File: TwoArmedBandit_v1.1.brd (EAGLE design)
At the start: 165.1 x 101.6 mm, 37 parts, among them J1 Nose_L, J10 LED_L, J11 Nose_R, J12 Lick_R, J13 Aux, J14 POWER_JACK, J15 Valve_R, J16 DAQ_L, J17 LED_R, J18 V_valve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

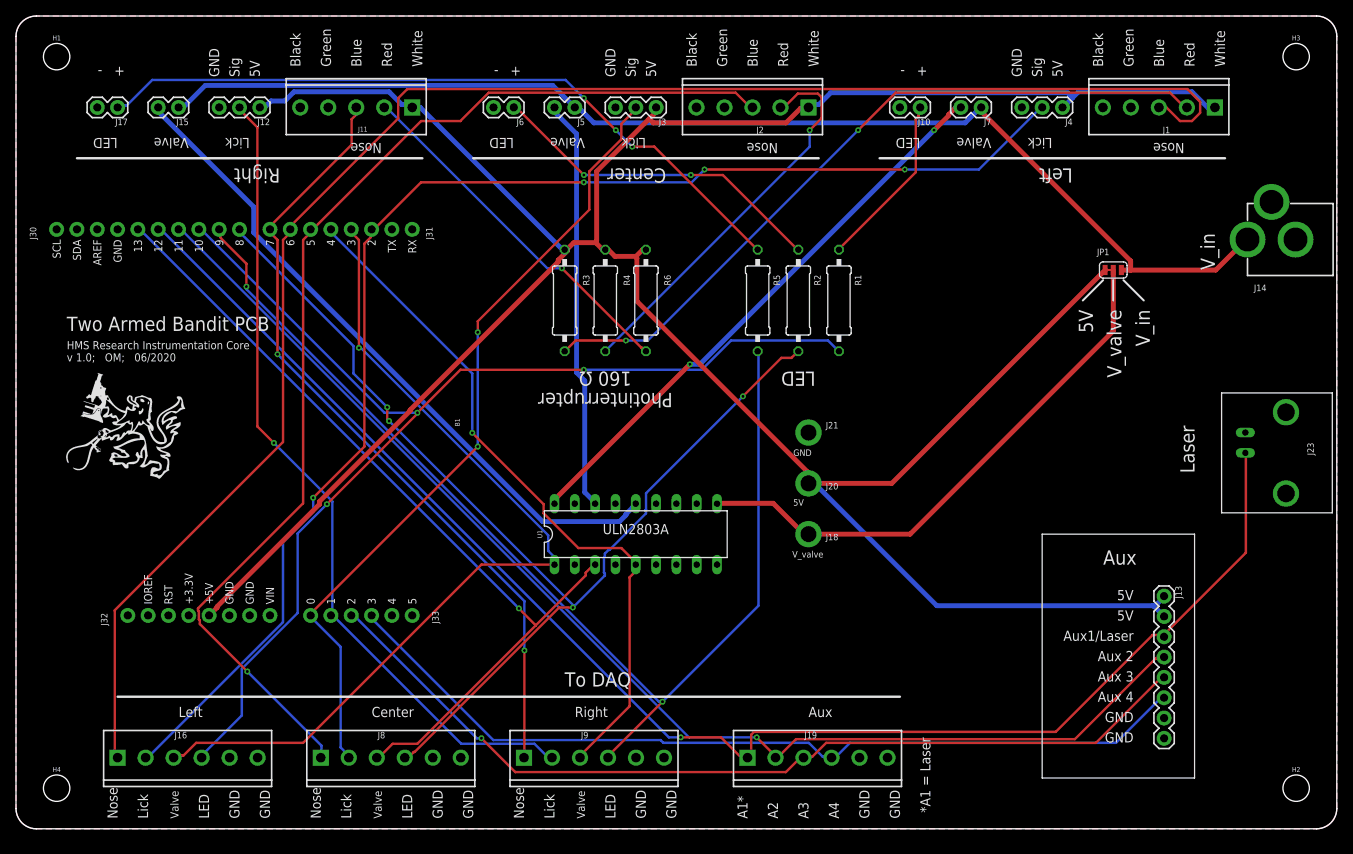
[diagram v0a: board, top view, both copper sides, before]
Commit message: Fix wiring of V_valve; Update version to v1.1
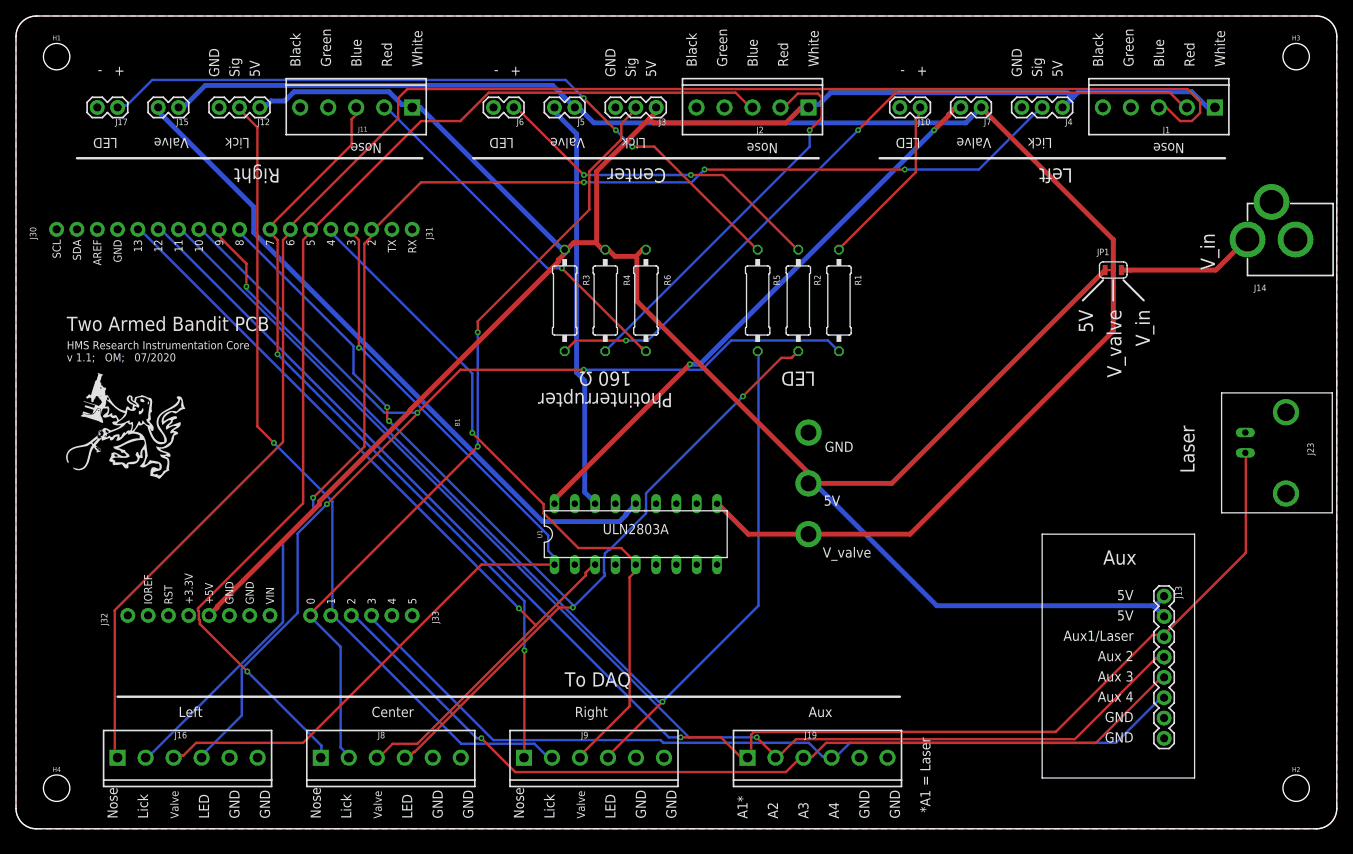
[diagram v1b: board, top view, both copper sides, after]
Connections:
- removed net VCC: J18.1, JP1.2, U1.10
- new net V_VALVE: J15.1, J18.1, J5.1, J7.1, JP1.2, U1.10
- net VIN: no longer J15.1, J5.1, J7.1
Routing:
- net V_VALVE: track 0.00 -> 200.6 mm
- net VIN: track 149.7 -> 17.4 mm
- net VCC: track 69.4 -> 0.00 mm
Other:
- board text added: "HMS Research Instrumentation Core v 1.1; OM; 07/2020"
- board text removed: "HMS Research Instrumentation Core v 1.0; OM; 06/2020"
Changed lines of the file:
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@@
 <text x="6.35" y="62.23" size="1.778" layer="21" font="vector" ratio="15">Two Armed Bandit PCB</text>
 <text x="6.35" y="58.42" size="1.016" layer="21" font="vector" ratio="13">HMS Research Instrumentation Core
-v 1.0;   OM;   06/2020</text>
+v 1.1;   OM;   07/2020</text>
 <text x="77.47" y="36.83" size="1.27" layer="21" font="vector" rot="SR0" align="bottom-center">ULN2803A</text>
 <text x="2.54" y="73.66" size="0.8128" layer="21" font="vector" ratio="15" rot="R90">J30</text>
@@
 </element>
 <element name="FRAME1" library="SparkFun-Aesthetics" library_urn="urn:adsk.eagle:library:507" package="DUMMY" package3d_urn="urn:adsk.eagle:package:37104/1" value="FRAME-LETTERNO_PACKAGE" x="-5.08" y="-2.54" smashed="yes" rot="R180">
-<attribute name="DESIGNER" value="Nobody" x="-5.08" y="-2.54" size="1.778" layer="27" rot="R180" display="off"/>
-<attribute name="VERSION" value="v01" x="-5.08" y="-2.54" size="1.778" layer="27" rot="R180" display="off"/>
+<attribute name="DESIGNER" value="Ofer Mazor" x="-5.08" y="-2.54" size="1.778" layer="27" rot="R180" display="off"/>
+<attribute name="VERSION" value="v01.1" x="-5.08" y="-2.54" size="1.778" layer="27" rot="R180" display="off"/>
 </element>
 <element name="J1" library="SparkFun-Connectors" library_urn="urn:adsk.eagle:library:513" package="SCREWTERMINAL-3.5MM-5" package3d_urn="urn:adsk.eagle:package:38112/1" value="Nose_L" x="149.86" y="90.17" smashed="yes" rot="R180">
@@
 </element>
 <element name="J18" library="SparkFun-Connectors" library_urn="urn:adsk.eagle:library:513" package="1X01_2MM" package3d_urn="urn:adsk.eagle:package:38029/1" value="V_valve" x="99.06" y="36.83" smashed="yes">
-<attribute name="NAME" x="101.219" y="36.068" size="0.8128" layer="25" font="vector" ratio="15"/>
-<attribute name="VALUE" x="97.028" y="33.909" size="0.8128" layer="21" font="vector" ratio="15"/>
+<attribute name="VALUE" x="100.838" y="33.909" size="1.27" layer="21" font="vector" ratio="15"/>
 </element>
 <element name="J20" library="SparkFun-Connectors" library_urn="urn:adsk.eagle:library:513" package="1X01_2MM" package3d_urn="urn:adsk.eagle:package:38029/1" value="5V" x="99.06" y="43.18" smashed="yes">
-<attribute name="NAME" x="101.219" y="42.418" size="0.8128" layer="25" font="vector" ratio="15"/>
-<attribute name="VALUE" x="97.155" y="40.386" size="0.8128" layer="21" font="vector" ratio="15"/>
+<attribute name="VALUE" x="100.965" y="40.386" size="1.27" layer="21" font="vector" ratio="15"/>
 </element>
 <element name="J21" library="SparkFun-Connectors" library_urn="urn:adsk.eagle:library:513" package="1X01_2MM" package3d_urn="urn:adsk.eagle:package:38029/1" value="GND" x="99.06" y="49.53" smashed="yes">
-<attribute name="NAME" x="101.219" y="50.038" size="0.8128" layer="25" font="vector" ratio="15"/>
-<attribute name="VALUE" x="97.155" y="46.609" size="0.8128" layer="21" font="vector" ratio="15"/>
+<attribute name="VALUE" x="101.092" y="47.117" size="1.27" layer="21" font="vector" ratio="15"/>
 </element>
 <element name="H1" library="SparkFun-Hardware" library_urn="urn:adsk.eagle:library:519" package="STAND-OFF" package3d_urn="urn:adsk.eagle:package:38630/1" value="STAND-OFF" x="5.08" y="96.52" smashed="yes">
@@
 <signal name="VIN" class="1">
 <contactref element="J14" pad="PWR"/>
-<contactref element="J7" pad="1"/>
-<contactref element="J5" pad="1"/>
-<contactref element="J15" pad="1"/>
 <contactref element="JP1" pad="1"/>
-<wire x1="20.9169" y1="90.1827" x2="20.3454" y2="90.1827" width="0.6096" layer="16"/>
-<wire x1="23.6601" y1="92.9259" x2="20.9169" y2="90.1827" width="0.6096" layer="16"/>
-<wire x1="67.0941" y1="92.9259" x2="23.6601" y2="92.9259" width="0.6096" layer="16"/>
-<wire x1="69.85" y1="90.17" x2="67.0941" y2="92.9259" width="0.6096" layer="16"/>
-<wire x1="20.3454" y1="90.1827" x2="20.32" y2="90.17" width="0.6096" layer="16"/>
 <wire x1="149.9616" y1="69.8373" x2="139.3317" y2="69.8373" width="0.6096" layer="1"/>
 <wire x1="139.3317" y1="69.8373" x2="138.1887" y2="69.8373" width="0.6096" layer="1"/>
@@
 <wire x1="138.1887" y1="69.8373" x2="138.176" y2="69.85" width="0.6096" layer="1"/>
 <wire x1="153.8478" y1="73.7235" x2="153.94" y2="73.66" width="0.6096" layer="1"/>
-<wire x1="120.7008" y1="89.6112" x2="120.7008" y2="90.0684" width="0.6096" layer="1"/>
-<wire x1="139.3317" y1="70.9803" x2="120.7008" y2="89.6112" width="0.6096" layer="1"/>
-<wire x1="139.3317" y1="69.8373" x2="139.3317" y2="70.9803" width="0.6096" layer="1"/>
-<wire x1="120.7008" y1="90.0684" x2="120.65" y2="90.17" width="0.6096" layer="1"/>
-<wire x1="70.4088" y1="90.0684" x2="70.0659" y2="90.0684" width="0.6096" layer="16"/>
-<wire x1="72.2376" y1="88.2396" x2="70.4088" y2="90.0684" width="0.6096" layer="16"/>
-<wire x1="118.6434" y1="88.2396" x2="72.2376" y2="88.2396" width="0.6096" layer="16"/>
-<wire x1="120.5865" y1="90.1827" x2="118.6434" y2="88.2396" width="0.6096" layer="16"/>
-<wire x1="70.0659" y1="90.0684" x2="69.85" y2="90.17" width="0.6096" layer="16"/>
-<wire x1="120.5865" y1="90.1827" x2="120.65" y2="90.17" width="0.6096" layer="16"/>
 </signal>
 <signal name="5V" class="1">
@@
 <via x="70.9803" y="91.3257" extent="1-16" drill="0.35"/>
 </signal>
-<signal name="VCC" class="1">
+<signal name="V_VALVE" class="1">
+<contactref element="U1" pad="10"/>
+<wire x1="87.6681" y1="40.6908" x2="87.63" y2="40.64" width="0.6096" layer="1"/>
+<wire x1="111.76" y1="36.83" x2="137.16" y2="62.23" width="0.6096" layer="1"/>
+<contactref element="J5" pad="1"/>
+<wire x1="70.4088" y1="90.0684" x2="70.0659" y2="90.0684" width="0.6096" layer="16"/>
+<wire x1="70.4088" y1="90.0684" x2="72.2376" y2="88.2396" width="0.6096" layer="16"/>
+<wire x1="70.0659" y1="90.0684" x2="69.85" y2="90.17" width="0.6096" layer="16"/>
+<contactref element="J7" pad="1"/>
+<contactref element="J15" pad="1"/>
+<wire x1="20.9169" y1="90.1827" x2="20.3454" y2="90.1827" width="0.6096" layer="16"/>
+<wire x1="23.6601" y1="92.9259" x2="20.9169" y2="90.1827" width="0.6096" layer="16"/>
+<wire x1="67.0941" y1="92.9259" x2="23.6601" y2="92.9259" width="0.6096" layer="16"/>
+<wire x1="20.3454" y1="90.1827" x2="20.32" y2="90.17" width="0.6096" layer="16"/>
 <contactref element="JP1" pad="2"/>
 <contactref element="J18" pad="1"/>
-<contactref element="U1" pad="10"/>
-<wire x1="94.6404" y1="40.6908" x2="87.6681" y2="40.6908" width="0.6096" layer="1"/>
-<wire x1="98.4123" y1="36.9189" x2="94.6404" y2="40.6908" width="0.6096" layer="1"/>
-<wire x1="98.9838" y1="36.9189" x2="98.4123" y2="36.9189" width="0.6096" layer="1"/>
-<wire x1="87.6681" y1="40.6908" x2="87.63" y2="40.64" width="0.6096" layer="1"/>
-<wire x1="98.9838" y1="36.9189" x2="99.06" y2="36.83" width="0.6096" layer="1"/>
-<wire x1="137.16" y1="69.85" x2="137.16" y2="62.23" width="0.6096" layer="1"/>
-<wire x1="137.16" y1="62.23" x2="111.76" y2="36.83" width="0.6096" layer="1"/>
-<wire x1="111.76" y1="36.83" x2="99.0727" y2="36.83" width="0.6096" layer="1"/>
-<wire x1="99.0727" y1="36.83" x2="98.9838" y2="36.9189" width="0.6096" layer="1"/>
+<wire x1="91.5289" y1="36.83" x2="87.6681" y2="40.6908" width="0.6096" layer="1"/>
+<wire x1="69.85" y1="90.17" x2="67.0941" y2="92.9259" width="0.6096" layer="16"/>
+<wire x1="99.06" y1="36.83" x2="91.5289" y2="36.83" width="0.6096" layer="1"/>
+<wire x1="99.06" y1="36.83" x2="111.76" y2="36.83" width="0.6096" layer="1"/>
+<wire x1="120.65" y1="90.17" x2="137.16" y2="73.66" width="0.6096" layer="1"/>
+<wire x1="118.7196" y1="88.2396" x2="120.65" y2="90.17" width="0.6096" layer="16"/>
+<wire x1="72.2376" y1="88.2396" x2="118.7196" y2="88.2396" width="0.6096" layer="16"/>
+<wire x1="137.16" y1="70.4342" x2="137.16" y2="73.66" width="0.6096" layer="1"/>
+<wire x1="137.16" y1="62.23" x2="137.16" y2="69.85" width="0.6096" layer="1"/>
+<wire x1="137.16" y1="70.4342" x2="137.16" y2="69.85" width="0.6096" layer="1"/>
 </signal>
 </signals>

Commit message: Swap pins for Aux-1/Aux-2
In order for Aux-1-Laser to have PWM, needed to change
Aux-1 to D11 and Aux-2 to D12.
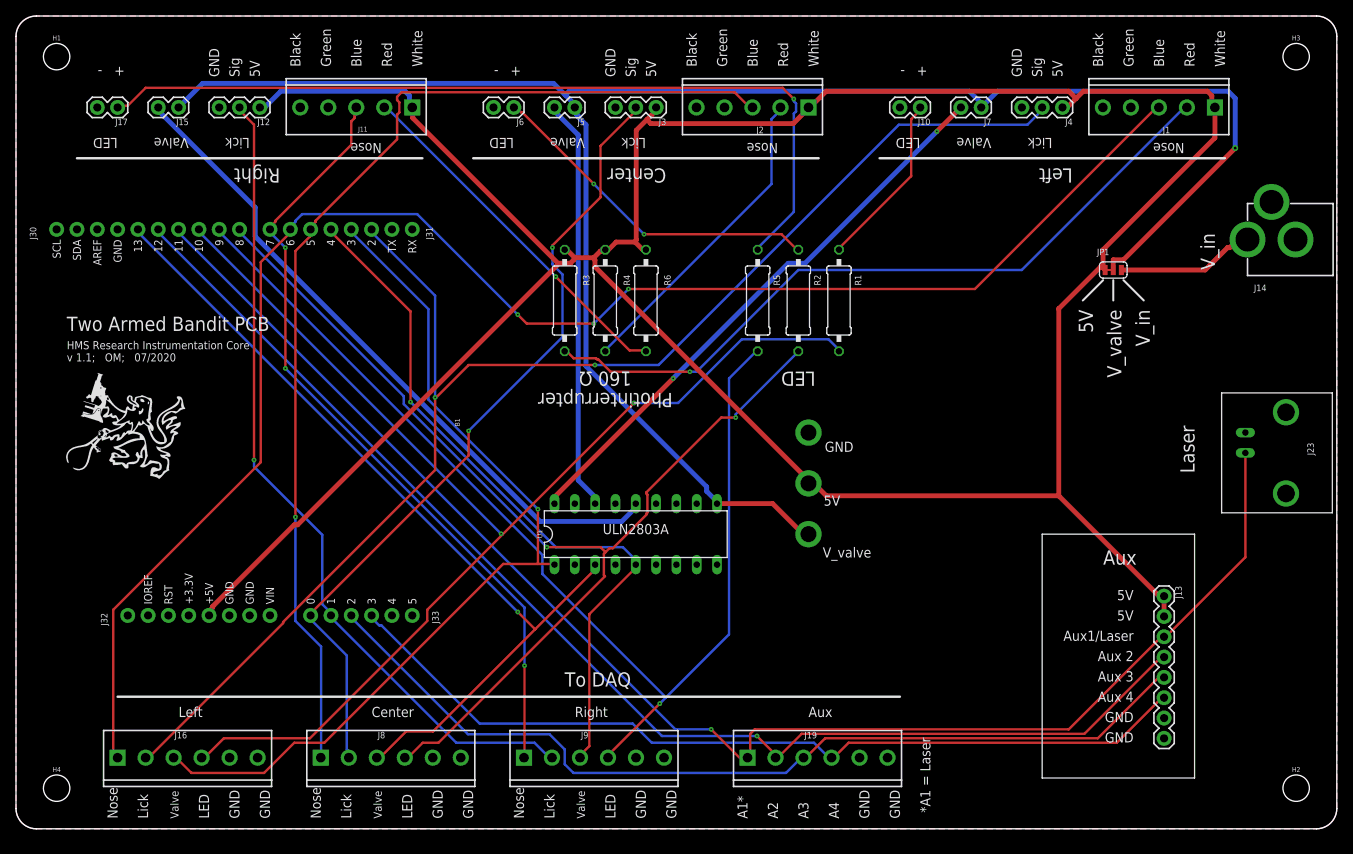
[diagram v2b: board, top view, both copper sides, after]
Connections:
- net AUX_1_LASER: now also B1.D11; no longer B1.D12
- net AUX_2: now also B1.D12; no longer B1.D11
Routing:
- net V_VALVE: track 200.6 -> 236.3 mm, vias 0 -> 1
- net N$5: track 90.3 -> 107.1 mm, vias 3 -> 1
- net 5V: track 357.7 -> 369.9 mm
- net N$1: track 49.0 -> 39.5 mm, vias 1 -> 0
- net LED_L: track 148.2 -> 156.8 mm, vias 3 -> 2
- net LICK_L: track 168.0 -> 175.7 mm, vias 4 -> 2
- net NOSE_C: track 141.4 -> 134.9 mm
- net NOSE_L: track 206.3 -> 201.9 mm, vias 0 -> 3
- net AUX_2: track 156.0 -> 159.0 mm
- net AUX_1_LASER: track 188.4 -> 186.1 mm
- net VALVE_R: track 87.8 -> 89.6 mm
- net AUX_3: track 114.6 -> 115.9 mm, vias 1 -> 0
- net LICK_C: track 100.2 -> 101.2 mm
- net LED_C: track 138.1 -> 137.3 mm, vias 4 -> 2
- net LED_R: track 141.0 -> 140.3 mm, vias 2 -> 1
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
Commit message: Add optional RC filter to lick sensor output
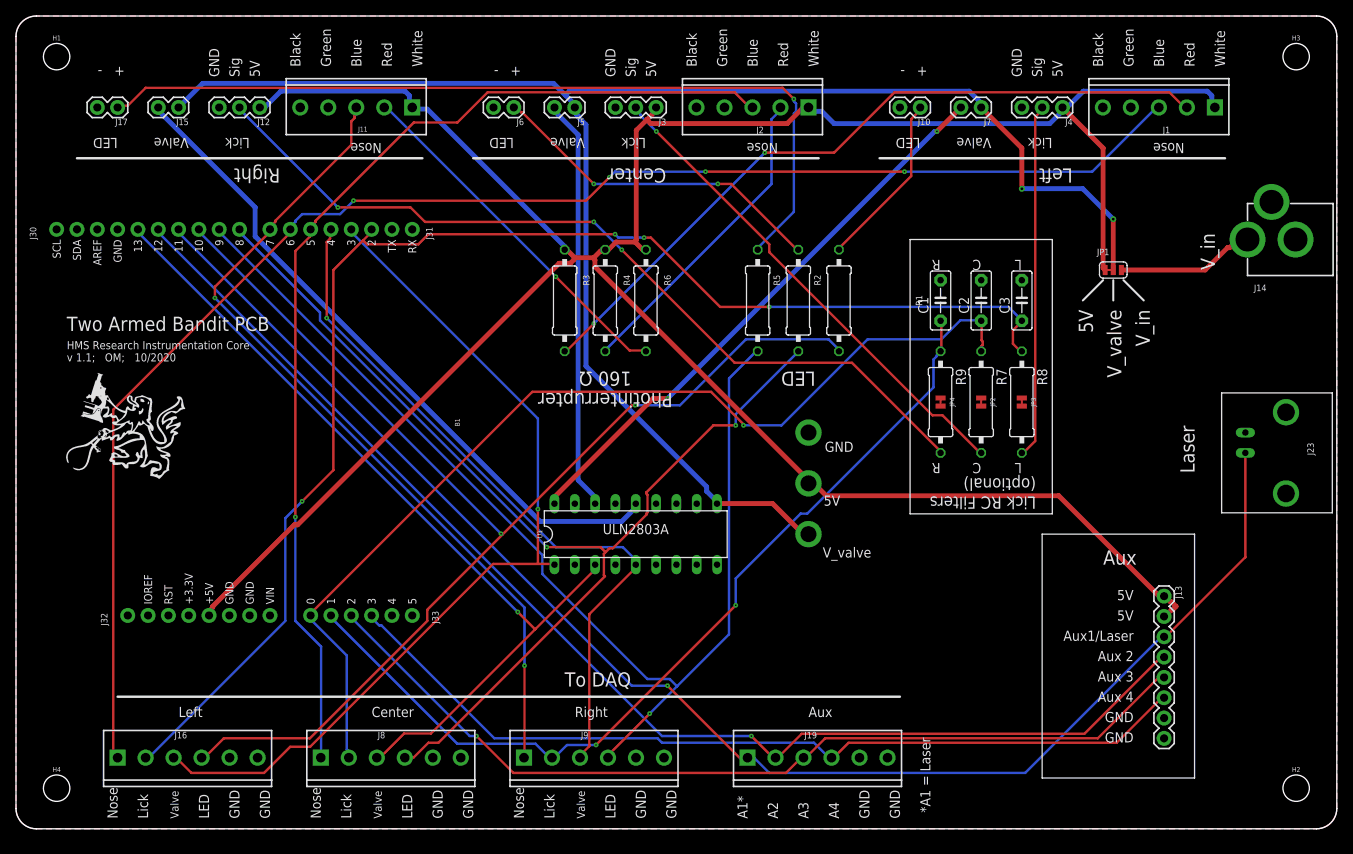
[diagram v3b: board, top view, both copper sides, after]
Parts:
- added C1, C2, C3: (no value), capacitor-wima:C5B2.5
- added JP2, JP3, JP4: JUMPER-SMT_2_NC_TRACE_NO-SILK, SparkFun-Jumpers:SMT-JUMPER_2_NC_TRACE_NO-SILK
- added R7, R8, R9: 160, rcl:0309/12
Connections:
- new net N$6: J12.2, JP4.2, R9.2
- new net N$7: J3.2, JP2.2, R7.2
- new net N$8: J4.2, JP3.2, R8.2
- net GND: now also C1.2, C2.2, C3.2
- net LICK_C: now also C2.1, JP2.1, R7.1; no longer J3.2
- net LICK_L: now also C3.1, JP3.1, R8.1; no longer J4.2
- net LICK_R: now also C1.1, JP4.1, R9.1; no longer J12.2
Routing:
- net N$6: track 0.00 -> 105.7 mm, vias 0 -> 3
- net N$7: track 0.00 -> 61.9 mm, vias 0 -> 1
- net N$8: track 0.00 -> 44.4 mm
- net 5V: track 369.9 -> 335.0 mm
- net V_VALVE: track 236.3 -> 206.4 mm, vias 1 -> 2
- net LICK_C: track 101.2 -> 126.6 mm, vias 2 -> 1
- net NOSE_L: track 201.9 -> 190.6 mm, vias 3 -> 4
- net LICK_R: track 103.4 -> 112.7 mm, vias 1 -> 2
- net NOSE_R: track 99.0 -> 104.7 mm, vias 3 -> 2
- net LICK_L: track 175.7 -> 170.5 mm, vias 2 -> 4
- net NOSE_C: track 134.9 -> 131.5 mm
- net AUX_3: track 115.9 -> 114.9 mm, vias 0 -> 1
- net LED_R: track 140.3 -> 141.1 mm
- net LED_C: track 137.3 -> 137.9 mm
- net N$2: track 92.5 -> 92.0 mm, vias 1 -> 2
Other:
- board text added: "C"
- board text added: "HMS Research Instrumentation Core v 1.1; OM; 10/2020"
- board text added: "L"
- board text added: "Lick RC Filters (optional)"
- board text added: "R"
- board text removed: "HMS Research Instrumentation Core v 1.1; OM; 07/2020"
